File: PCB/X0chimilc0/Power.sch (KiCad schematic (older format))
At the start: 1 part

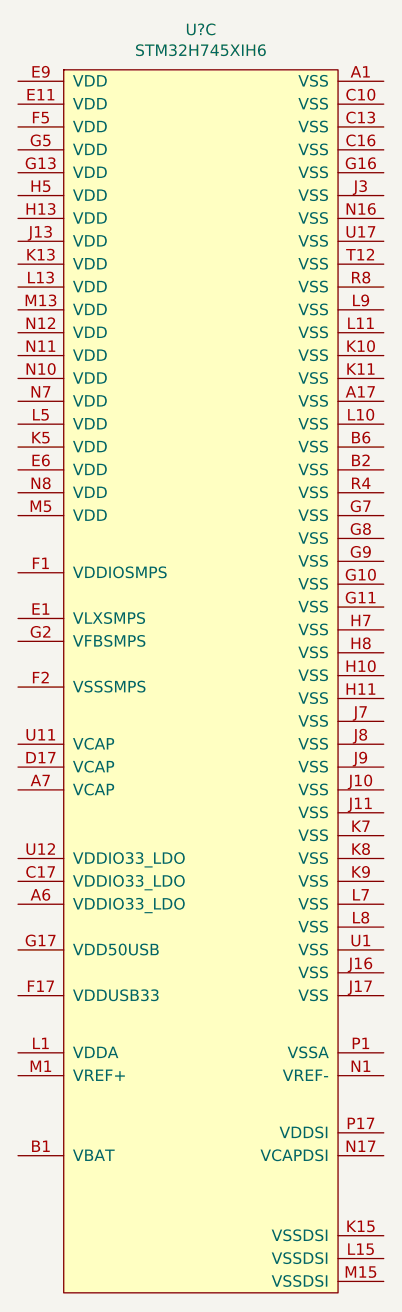
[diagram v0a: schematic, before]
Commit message: PCB Mockup
Made components for DAC/MCU/FPGA/Connectors, mocked things up as PCB, going to be crazy.
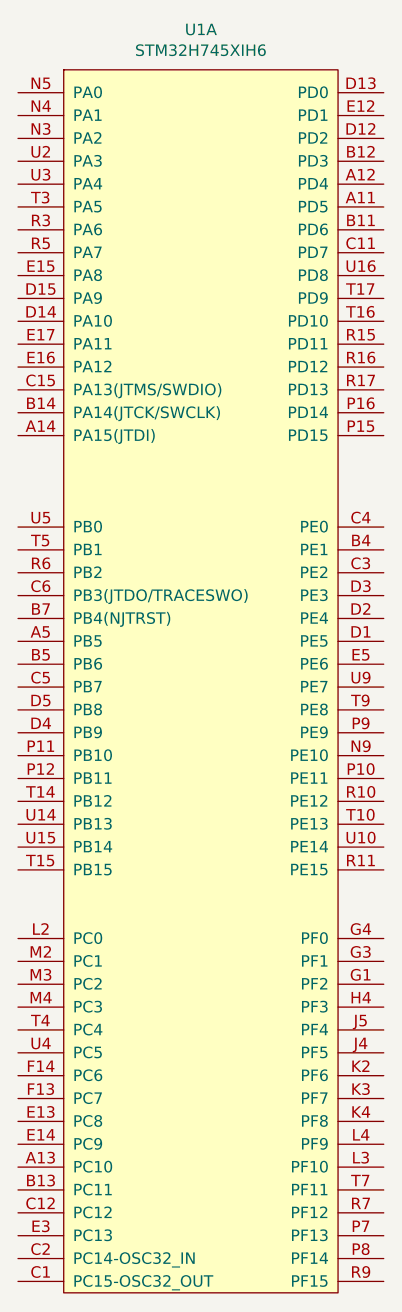
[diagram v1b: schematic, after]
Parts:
- gave numbers to parts that had none: 1
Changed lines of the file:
@@
 $EndDescr
 $Comp
-L AVR-KiCAD-Lib-ICs:STM32H745XIH6 U?
-U 3 1 5E2FFF04
+L AVR-KiCAD-Lib-ICs:STM32H745XIH6 U1
+U 1 1 5E2FFF04
 P 8550 1000
-F 0 "U?" H 8150 1175 50  0000 C CNN
+F 0 "U1" H 8150 1175 50  0000 C CNN
 F 1 "STM32H745XIH6" H 8600 1200 50  0001 C CNN
 F 2 "AVR-KiCAD-Lib-ICs:STM32H745XIH6" H 8350 1000 50  0001 C CNN
@@
 F 27 "STM32H745XIH6" H 8150 1084 50  0000 C CNN "_Value_"
 F 28 "*" H 10950 3600 50  0001 C CNN "Management_ID"
-	3    8550 1000
+	1    8550 1000
 	1    0    0    -1
 $EndComp

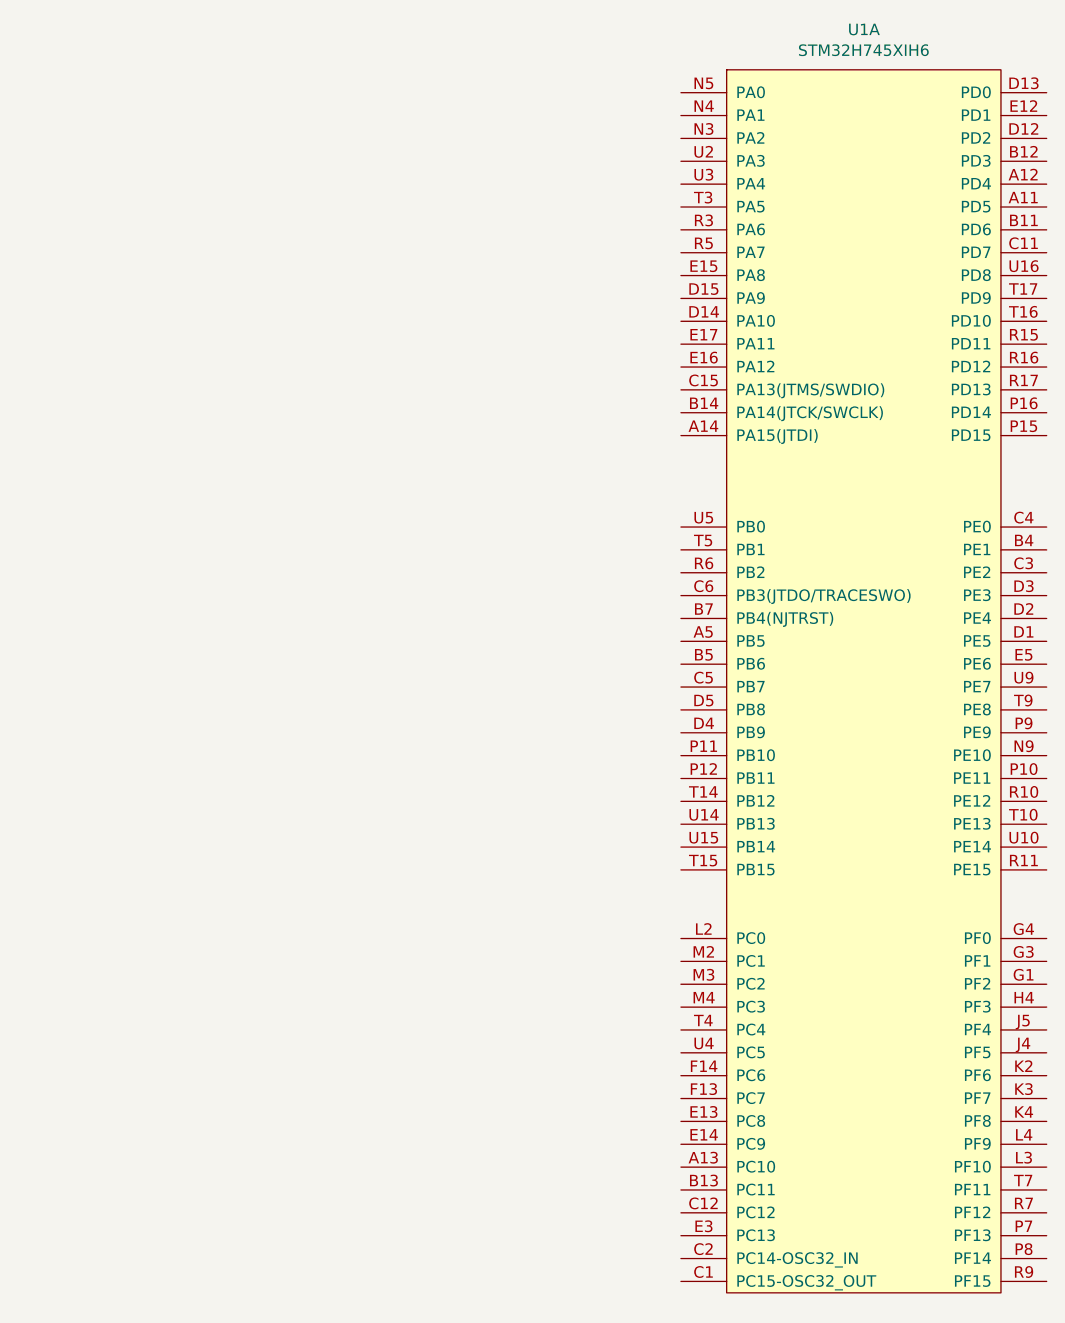
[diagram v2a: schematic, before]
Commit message: Component PDFs
added relevant PDF datasheets and some minor schematic edits
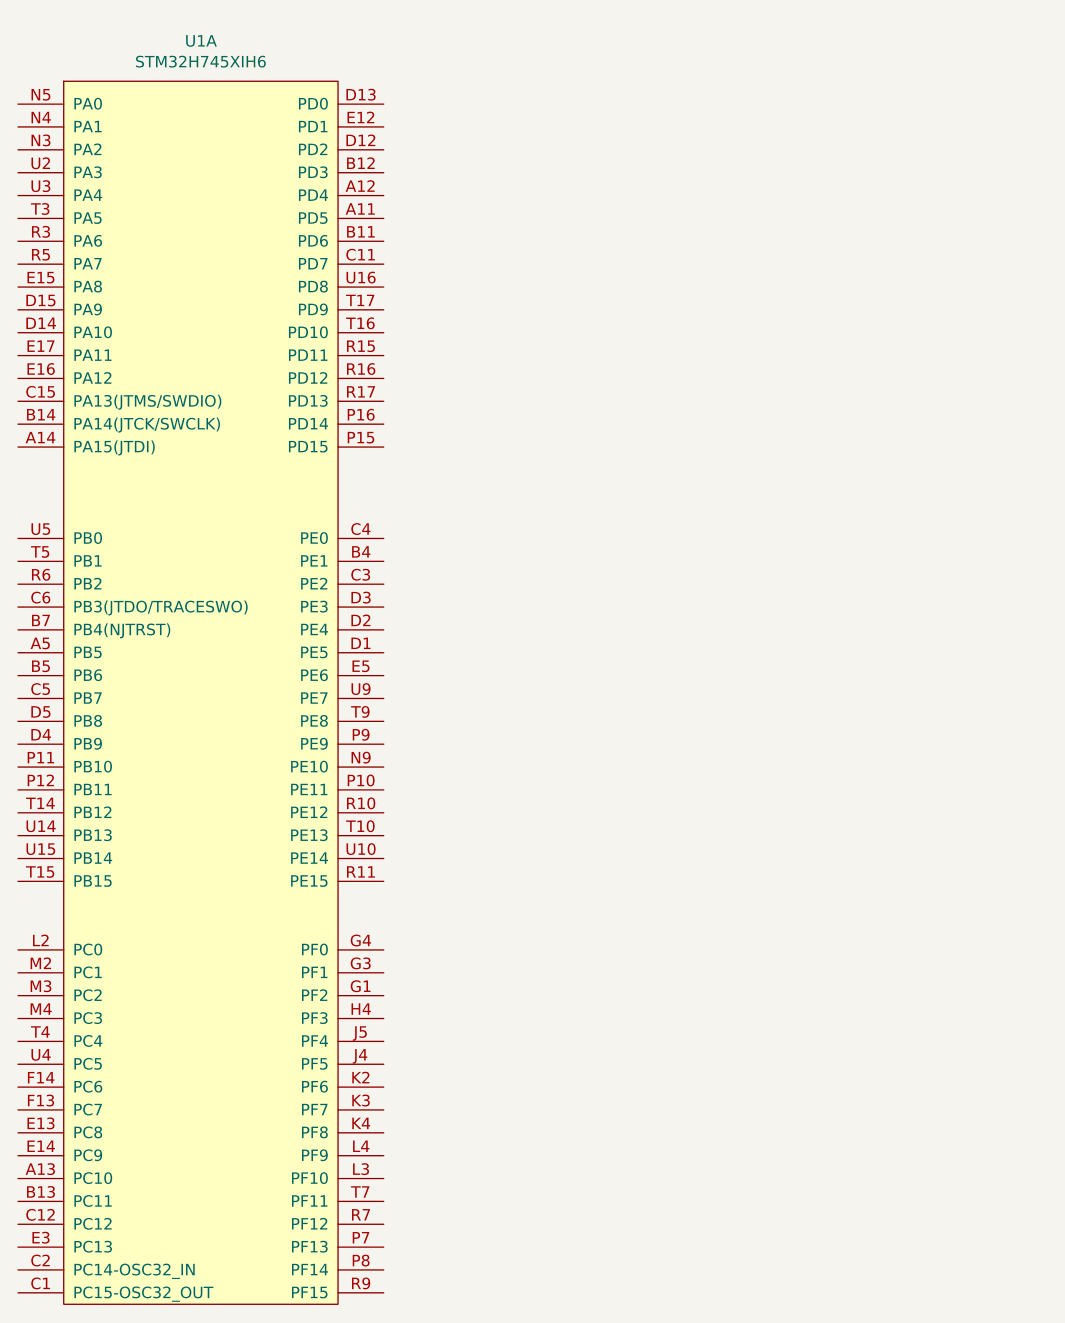
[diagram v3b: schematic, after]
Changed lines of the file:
@@
 $Comp
 L AVR-KiCAD-Lib-ICs:STM32H745XIH6 U1
-U 1 1 5E2FFF04
-P 8550 1000
-F 0 "U1" H 8150 1175 50  0000 C CNN
-F 1 "STM32H745XIH6" H 8600 1200 50  0001 C CNN
-F 2 "AVR-KiCAD-Lib-ICs:STM32H745XIH6" H 8350 1000 50  0001 C CNN
-F 3 "https://www.st.com/resource/en/datasheet/stm32h745ii.pdf" H 8450 1100 50  0001 C CNN
-F 4 "17.02000" H 8650 1250 50  0001 C CNN "Cost QTY: 1"
-F 5 "11.75168" H 8750 1350 50  0001 C CNN "Cost QTY: 1000"
-F 6 "11.75168" H 8850 1450 50  0001 C CNN "Cost QTY: 2500"
-F 7 "11.75168" H 8950 1550 50  0001 C CNN "Cost QTY: 5000"
-F 8 "11.75168" H 9050 1650 50  0001 C CNN "Cost QTY: 10000"
-F 9 "STMicroelectronics" H 9150 1750 50  0001 C CNN "MFR"
-F 10 "STM32H745XIH6" H 9250 1850 50  0001 C CNN "MFR#"
-F 11 "Digikey" H 9350 1950 50  0001 C CNN "Vendor"
-F 12 "497-19502-ND" H 9450 2050 50  0001 C CNN "Vendor #"
-F 13 "AVR" H 9550 2150 50  0001 C CNN "Designer"
-F 14 "0.76mm" H 9650 2250 50  0001 C CNN "Height"
-F 15 "11/29/2019" H 10750 3350 50  0001 C CNN "Date Created"
-F 16 "11/29/2019" H 9750 2350 50  0001 C CNN "Date Modified"
-F 17 "Yes" H 9850 2450 50  0001 C CNN "Lead-Free ?"
-F 18 "1" H 9950 2550 50  0001 C CNN "RoHS Levels"
-F 19 "SMT" H 10050 2650 50  0001 C CNN "Mounting"
-F 20 "265" H 10150 2750 50  0001 C CNN "Pin Count #"
-F 21 "Active" H 10250 2850 50  0001 C CNN "Status"
-F 22 "*" H 10350 2950 50  0001 C CNN "Tolerance"
-F 23 "Microcontroller Dual Core" H 10450 3050 50  0001 C CNN "Type"
-F 24 "3.3V" H 10550 3150 50  0001 C CNN "Voltage"
-F 25 "BGA" H 10650 3300 50  0001 C CNN "Package"
-F 26 "ARM® Cortex®-M4, Cortex®-M7 STM32H7 Microcontroller IC 32-Bit Dual-Core 240MHz, 480MHz 2MB (2M x 8) FLASH 240+25-TFBGA (14x14)" H 10950 3600 50  0001 C CNN "Description"
-F 27 "STM32H745XIH6" H 8150 1084 50  0000 C CNN "_Value_"
-F 28 "*" H 10950 3600 50  0001 C CNN "Management_ID"
-	1    8550 1000
+U 1 1 5DEFF51F
+P 5650 1050
+F 0 "U1" H 5250 1225 50  0000 C CNN
+F 1 "STM32H745XIH6" H 5700 1250 50  0001 C CNN
+F 2 "AVR-KiCAD-Lib-ICs:STM32H745XIH6" H 5450 1050 50  0001 C CNN
+F 3 "https://www.st.com/resource/en/datasheet/stm32h745ii.pdf" H 5550 1150 50  0001 C CNN
+F 4 "17.02000" H 5750 1300 50  0001 C CNN "Cost QTY: 1"
+F 5 "11.75168" H 5850 1400 50  0001 C CNN "Cost QTY: 1000"
+F 6 "11.75168" H 5950 1500 50  0001 C CNN "Cost QTY: 2500"
+F 7 "11.75168" H 6050 1600 50  0001 C CNN "Cost QTY: 5000"
+F 8 "11.75168" H 6150 1700 50  0001 C CNN "Cost QTY: 10000"
+F 9 "STMicroelectronics" H 6250 1800 50  0001 C CNN "MFR"
+F 10 "STM32H745XIH6" H 6350 1900 50  0001 C CNN "MFR#"
+F 11 "Digikey" H 6450 2000 50  0001 C CNN "Vendor"
+F 12 "497-19502-ND" H 6550 2100 50  0001 C CNN "Vendor #"
+F 13 "AVR" H 6650 2200 50  0001 C CNN "Designer"
+F 14 "0.76mm" H 6750 2300 50  0001 C CNN "Height"
+F 15 "11/29/2019" H 7850 3400 50  0001 C CNN "Date Created"
+F 16 "11/29/2019" H 6850 2400 50  0001 C CNN "Date Modified"
+F 17 "Yes" H 6950 2500 50  0001 C CNN "Lead-Free ?"
+F 18 "1" H 7050 2600 50  0001 C CNN "RoHS Levels"
+F 19 "SMT" H 7150 2700 50  0001 C CNN "Mounting"
+F 20 "265" H 7250 2800 50  0001 C CNN "Pin Count #"
+F 21 "Active" H 7350 2900 50  0001 C CNN "Status"
+F 22 "*" H 7450 3000 50  0001 C CNN "Tolerance"
+F 23 "Microcontroller Dual Core" H 7550 3100 50  0001 C CNN "Type"
+F 24 "3.3V" H 7650 3200 50  0001 C CNN "Voltage"
+F 25 "BGA" H 7750 3350 50  0001 C CNN "Package"
+F 26 "ARM® Cortex®-M4, Cortex®-M7 STM32H7 Microcontroller IC 32-Bit Dual-Core 240MHz, 480MHz 2MB (2M x 8) FLASH 240+25-TFBGA (14x14)" H 8050 3650 50  0001 C CNN "Description"
+F 27 "STM32H745XIH6" H 5250 1134 50  0000 C CNN "_Value_"
+F 28 "*" H 8050 3650 50  0001 C CNN "Management_ID"
+	1    5650 1050
 	1    0    0    -1
 $EndComp

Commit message: MCU Power
MCU power schematic completed, working on other MCU part and Codec.
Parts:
- removed U1: STM32H745XIH6, AVR-KiCAD-Lib-ICs:STM32H745XIH6, symbol AVR-KiCAD-Lib-ICs:STM32H745XIH6
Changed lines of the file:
@@
 EELAYER 30 0
 EELAYER END
-$Descr A4 11693 8268
+$Descr A3 16535 11693
 encoding utf-8
-Sheet 2 7
+Sheet 2 8
 Title ""
 Date ""
@@
 Comment4 ""
 $EndDescr
-$Comp
-L AVR-KiCAD-Lib-ICs:STM32H745XIH6 U1
-U 1 1 5DEFF51F
-P 5650 1050
-F 0 "U1" H 5250 1225 50  0000 C CNN
-F 1 "STM32H745XIH6" H 5700 1250 50  0001 C CNN
-F 2 "AVR-KiCAD-Lib-ICs:STM32H745XIH6" H 5450 1050 50  0001 C CNN
-F 3 "https://www.st.com/resource/en/datasheet/stm32h745ii.pdf" H 5550 1150 50  0001 C CNN
-F 4 "17.02000" H 5750 1300 50  0001 C CNN "Cost QTY: 1"
-F 5 "11.75168" H 5850 1400 50  0001 C CNN "Cost QTY: 1000"
-F 6 "11.75168" H 5950 1500 50  0001 C CNN "Cost QTY: 2500"
-F 7 "11.75168" H 6050 1600 50  0001 C CNN "Cost QTY: 5000"
-F 8 "11.75168" H 6150 1700 50  0001 C CNN "Cost QTY: 10000"
-F 9 "STMicroelectronics" H 6250 1800 50  0001 C CNN "MFR"
-F 10 "STM32H745XIH6" H 6350 1900 50  0001 C CNN "MFR#"
-F 11 "Digikey" H 6450 2000 50  0001 C CNN "Vendor"
-F 12 "497-19502-ND" H 6550 2100 50  0001 C CNN "Vendor #"
-F 13 "AVR" H 6650 2200 50  0001 C CNN "Designer"
-F 14 "0.76mm" H 6750 2300 50  0001 C CNN "Height"
-F 15 "11/29/2019" H 7850 3400 50  0001 C CNN "Date Created"
-F 16 "11/29/2019" H 6850 2400 50  0001 C CNN "Date Modified"
-F 17 "Yes" H 6950 2500 50  0001 C CNN "Lead-Free ?"
-F 18 "1" H 7050 2600 50  0001 C CNN "RoHS Levels"
-F 19 "SMT" H 7150 2700 50  0001 C CNN "Mounting"
-F 20 "265" H 7250 2800 50  0001 C CNN "Pin Count #"
-F 21 "Active" H 7350 2900 50  0001 C CNN "Status"
-F 22 "*" H 7450 3000 50  0001 C CNN "Tolerance"
-F 23 "Microcontroller Dual Core" H 7550 3100 50  0001 C CNN "Type"
-F 24 "3.3V" H 7650 3200 50  0001 C CNN "Voltage"
-F 25 "BGA" H 7750 3350 50  0001 C CNN "Package"
-F 26 "ARM® Cortex®-M4, Cortex®-M7 STM32H7 Microcontroller IC 32-Bit Dual-Core 240MHz, 480MHz 2MB (2M x 8) FLASH 240+25-TFBGA (14x14)" H 8050 3650 50  0001 C CNN "Description"
-F 27 "STM32H745XIH6" H 5250 1134 50  0000 C CNN "_Value_"
-F 28 "*" H 8050 3650 50  0001 C CNN "Management_ID"
-	1    5650 1050
-	1    0    0    -1
-$EndComp
 $EndSCHEMATC
